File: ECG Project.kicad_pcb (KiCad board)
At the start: 2 copper layers, 64.8 x 34.3 mm, 12 parts, among them J1 Battery, J2 Conn_01x03_Pin, U1 AD620

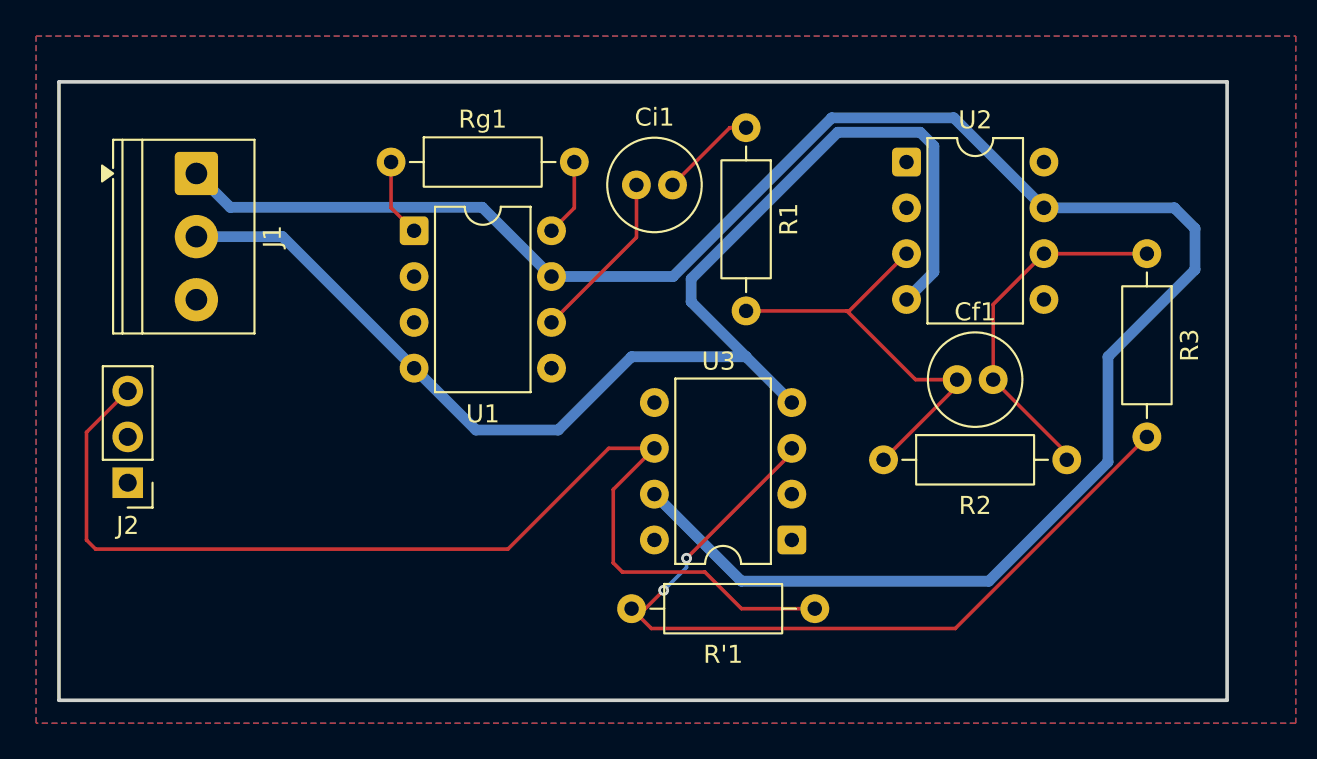
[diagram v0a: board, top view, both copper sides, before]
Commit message: Update U2-3 pinout and add milled labels
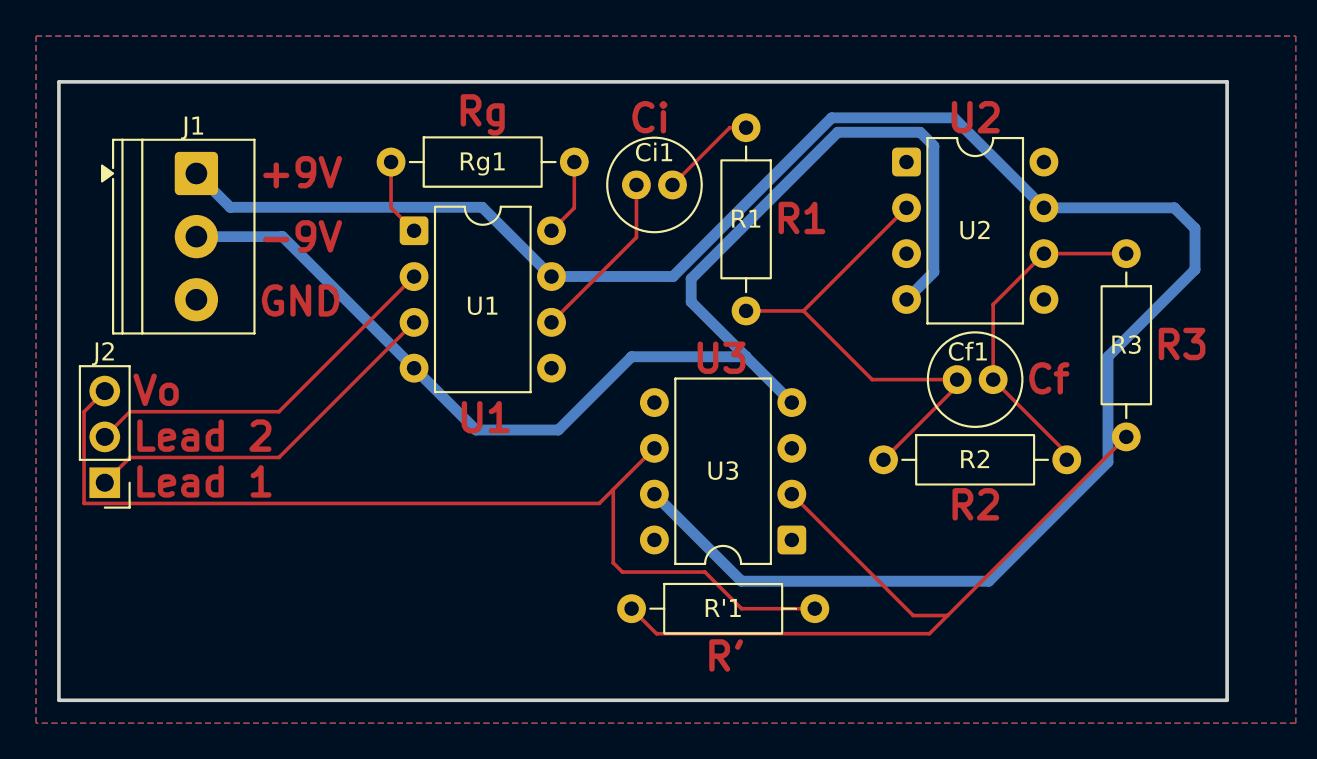
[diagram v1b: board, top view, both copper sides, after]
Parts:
- U2, U3: value ~ -> OP07
- moved J2 1.27 mm to (99.1, 88.3)
- moved R3 1.14 mm to (155.7, 75.6)
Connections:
- U2 pad 1: (no net) -> unconnected-(U2-VOS-Pad1)
- U2 pad 2: GNDREF -> Net-(U2--)
- U2 pad 3: Net-(U2--) -> GNDREF
- U2 pad 5: (no net) -> unconnected-(U2-NC-Pad5)
- U2 pad 8: (no net) -> unconnected-(U2-VOS-Pad8)
- U3 pad 1: (no net) -> unconnected-(U3-VOS-Pad1)
- U3 pad 2: GNDREF -> Net-(U3--)
- U3 pad 3: Net-(U3--) -> GNDREF
- U3 pad 5: (no net) -> unconnected-(U3-NC-Pad5)
- U3 pad 8: (no net) -> unconnected-(U3-VOS-Pad8)
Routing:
- net /Vi2: track 0.00 -> 20.8 mm
- net /Vi1: track 0.00 -> 20.8 mm
- net /Vo: track 62.7 -> 55.9 mm
- net Net-(U2--): track 24.0 -> 27.5 mm
- net Net-(U3--): track 46.5 -> 44.0 mm, vias 2 -> 0
- net Net-(Cf1-Pad2): track 20.0 -> 18.9 mm

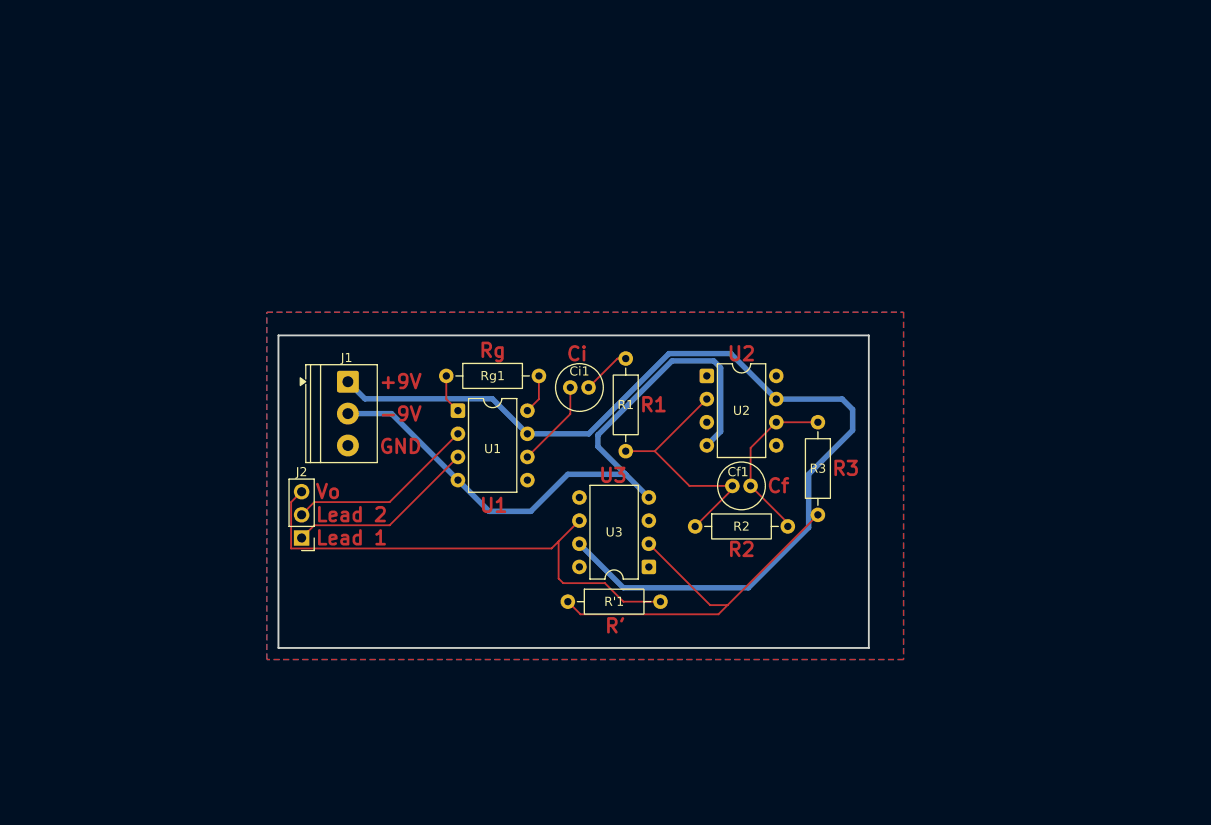
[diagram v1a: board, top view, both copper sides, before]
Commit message: Mounting Holes + More Clearance
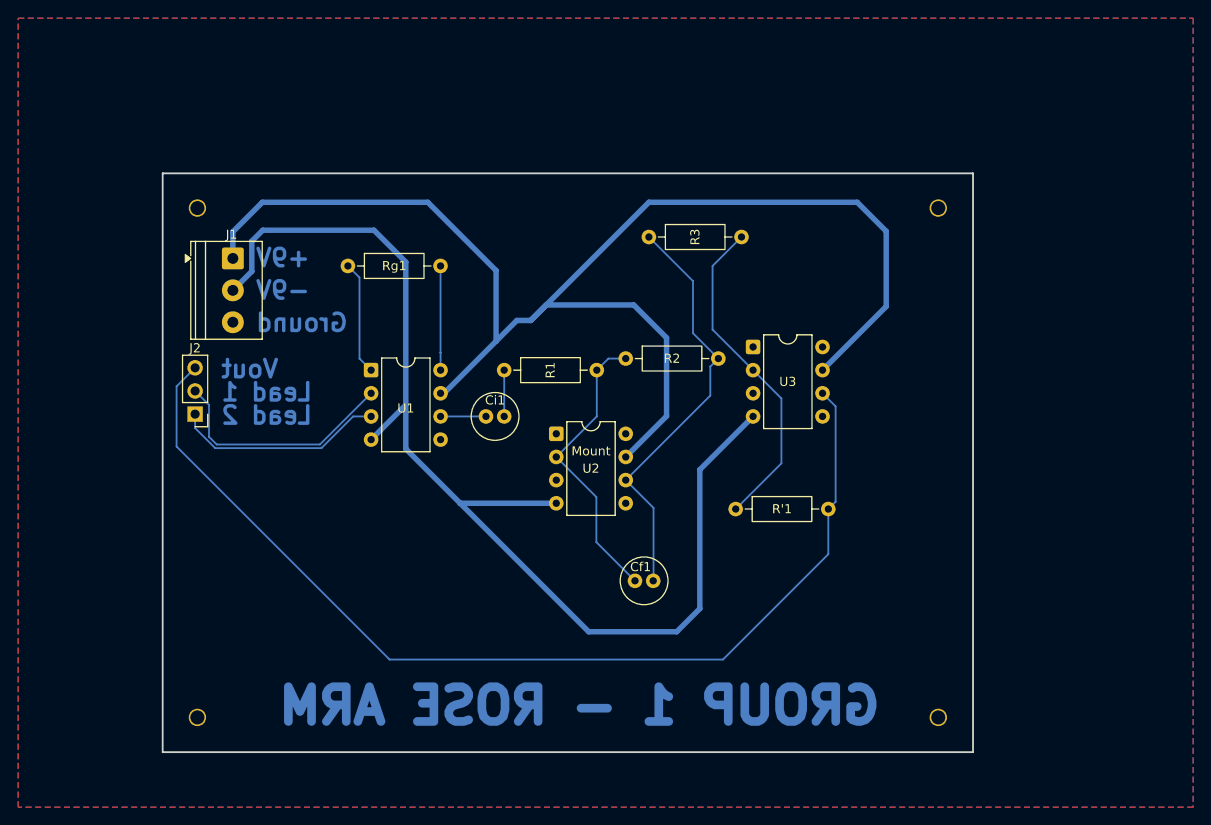
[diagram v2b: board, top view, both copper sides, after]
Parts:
- added Mount: Mounting Holes, Single Use:Untitled, F.Cu at (128.3, 80.0)
- moved R3 27.5 mm to (137.2, 55.2), turned to 0 degrees
- moved U3 26.7 mm to (148.6, 67.3), turned to 0 degrees
- moved R'1 21.0 mm to (146.7, 85.1)
- moved R2 19.9 mm to (134.6, 68.6)
- moved J1 18.5 mm to (91.5, 57.6)
- moved J2 17.9 mm to (87.4, 74.7)
- moved U2 17.7 mm to (127.0, 76.8)
- moved Rg1 16.2 mm to (104.1, 58.4)
- moved Cf1 14.9 mm to (135.6, 93.0)
- moved R1 13.4 mm to (121.3, 69.8), turned to 0 degrees
- moved U1 10.5 mm to (106.7, 69.8)
- moved Ci1 9.78 mm to (119.3, 74.9)
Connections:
- net /Vi1 renamed /Vi-
- net /Vi2 renamed /Vi+
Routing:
- net /Vo: track 55.9 -> 114.0 mm
- net -9V: track 72.1 -> 126.6 mm
- net +9V: track 108.8 -> 153.0 mm
- net Net-(Cf1-Pad2): track 18.9 -> 46.4 mm
- net Net-(Rg1-Pad1): track 4.34 -> 12.5 mm
- net Net-(U3--): track 44.0 -> 36.4 mm
- net Net-(Rg1-Pad2): track 4.33 -> 11.4 mm
- net /Vi+: track 20.8 -> 26.1 mm
- net Net-(U2--): track 27.5 -> 32.2 mm
- net Net-(Ci1-Pad1): track 9.57 -> 4.98 mm
- net /Vi-: track 20.8 -> 23.2 mm
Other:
- board size 64.8 x 34.3 mm -> 88.9 x 63.5 mm
- board text added: "2.2 in"
- board text added: "3.2 in"

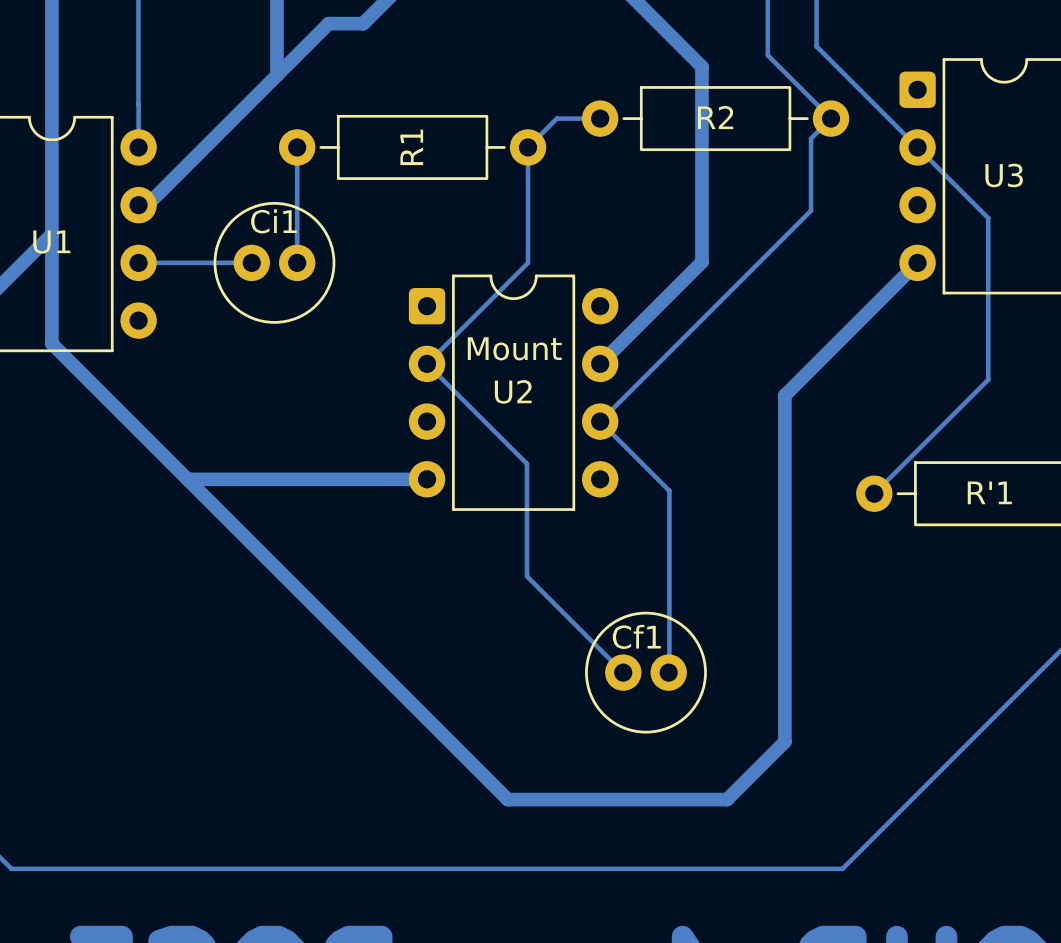
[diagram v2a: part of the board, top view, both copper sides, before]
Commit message: Changed capacitor sizes
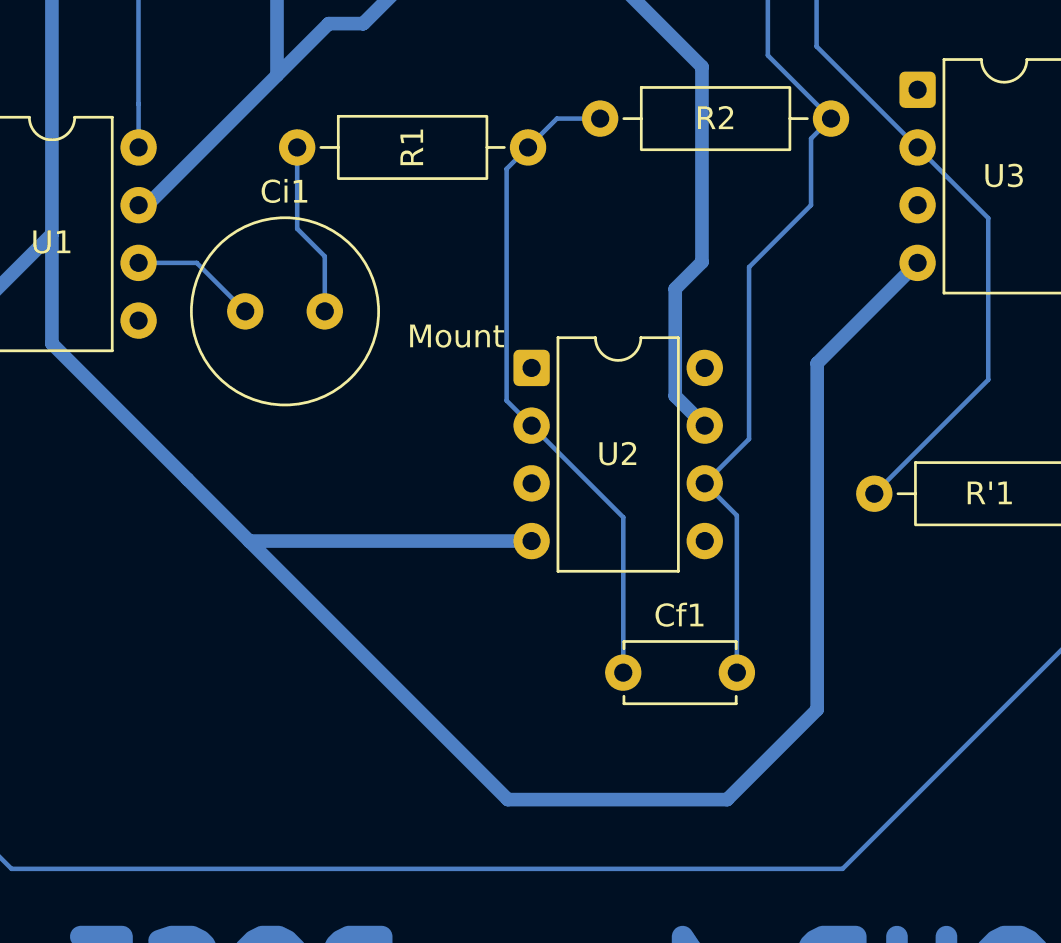
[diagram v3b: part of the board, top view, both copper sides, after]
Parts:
- Cf1: footprint Capacitor_THT:C_Radial_D5.0mm_H11.0mm_P2.00mm -> Capacitor_THT:C_Disc_D4.7mm_W2.5mm_P5.00mm
- Ci1: footprint Capacitor_THT:C_Radial_D5.0mm_H11.0mm_P2.00mm -> Capacitor_THT:C_Radial_D8.0mm_H11.5mm_P3.50mm
- moved U2 5.34 mm to (131.6, 79.6)
- moved Ci1 2.15 mm to (119.0, 77.1)
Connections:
- net /Vi+ renamed /Vi2
- net /Vi- renamed /Vi1
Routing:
- net Net-(U2--): track 32.2 -> 29.3 mm
- net Net-(Ci1-Pad2): track 5.08 -> 7.72 mm
- net Net-(Cf1-Pad2): track 46.4 -> 43.8 mm
- net +9V: track 153.0 -> 154.9 mm
- net -9V: track 126.6 -> 128.5 mm
- net Net-(Ci1-Pad1): track 4.98 -> 5.58 mm
